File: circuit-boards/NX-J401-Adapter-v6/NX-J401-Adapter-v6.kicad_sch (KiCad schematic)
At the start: 19 parts, among them J1 NX BUTTON, J2 POWER, J3 USB1, J4 USB2, J5 CAN1, J6 CAN1, J7 15V, Q1 SQM120P06-07L_GE3, SW1 RECOVERY, SW2 RESET

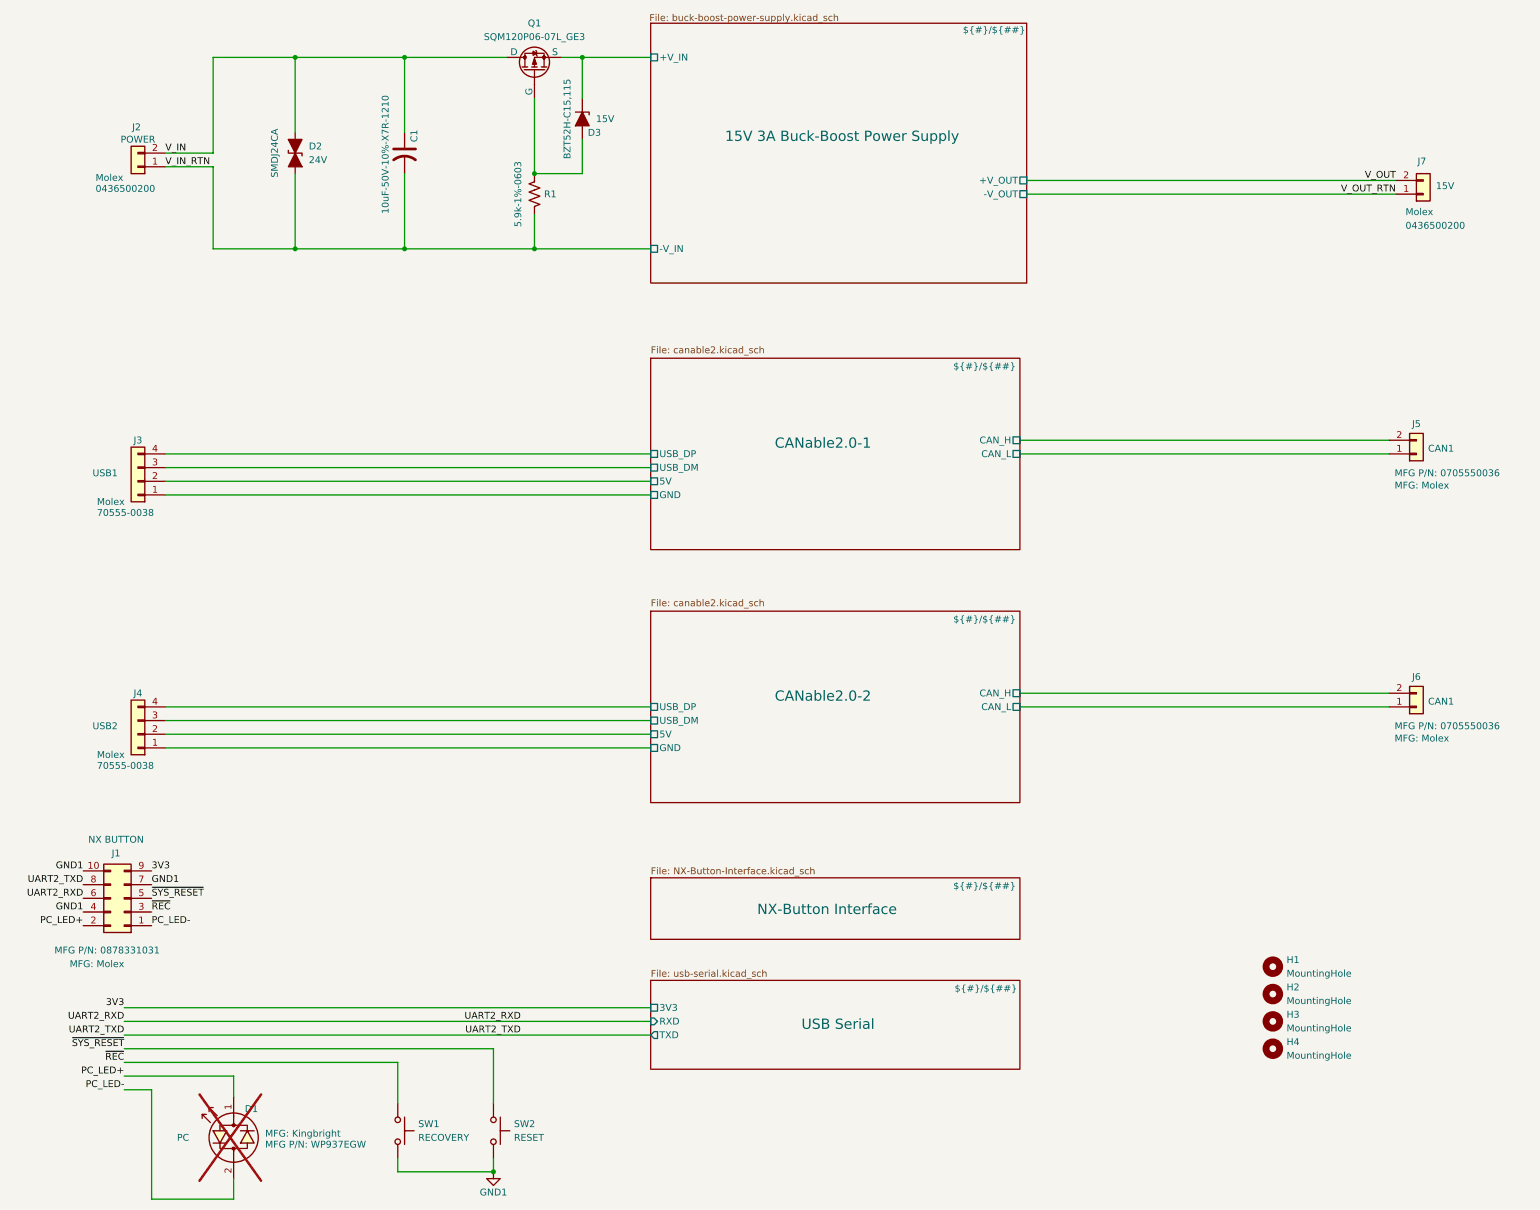
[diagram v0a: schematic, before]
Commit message: Changed canable to use 3.3V power form USB to use key-e connector that breaks out USB and 3V3
Signed-off-by: Scott Berman <sgberman1@gmail.com>
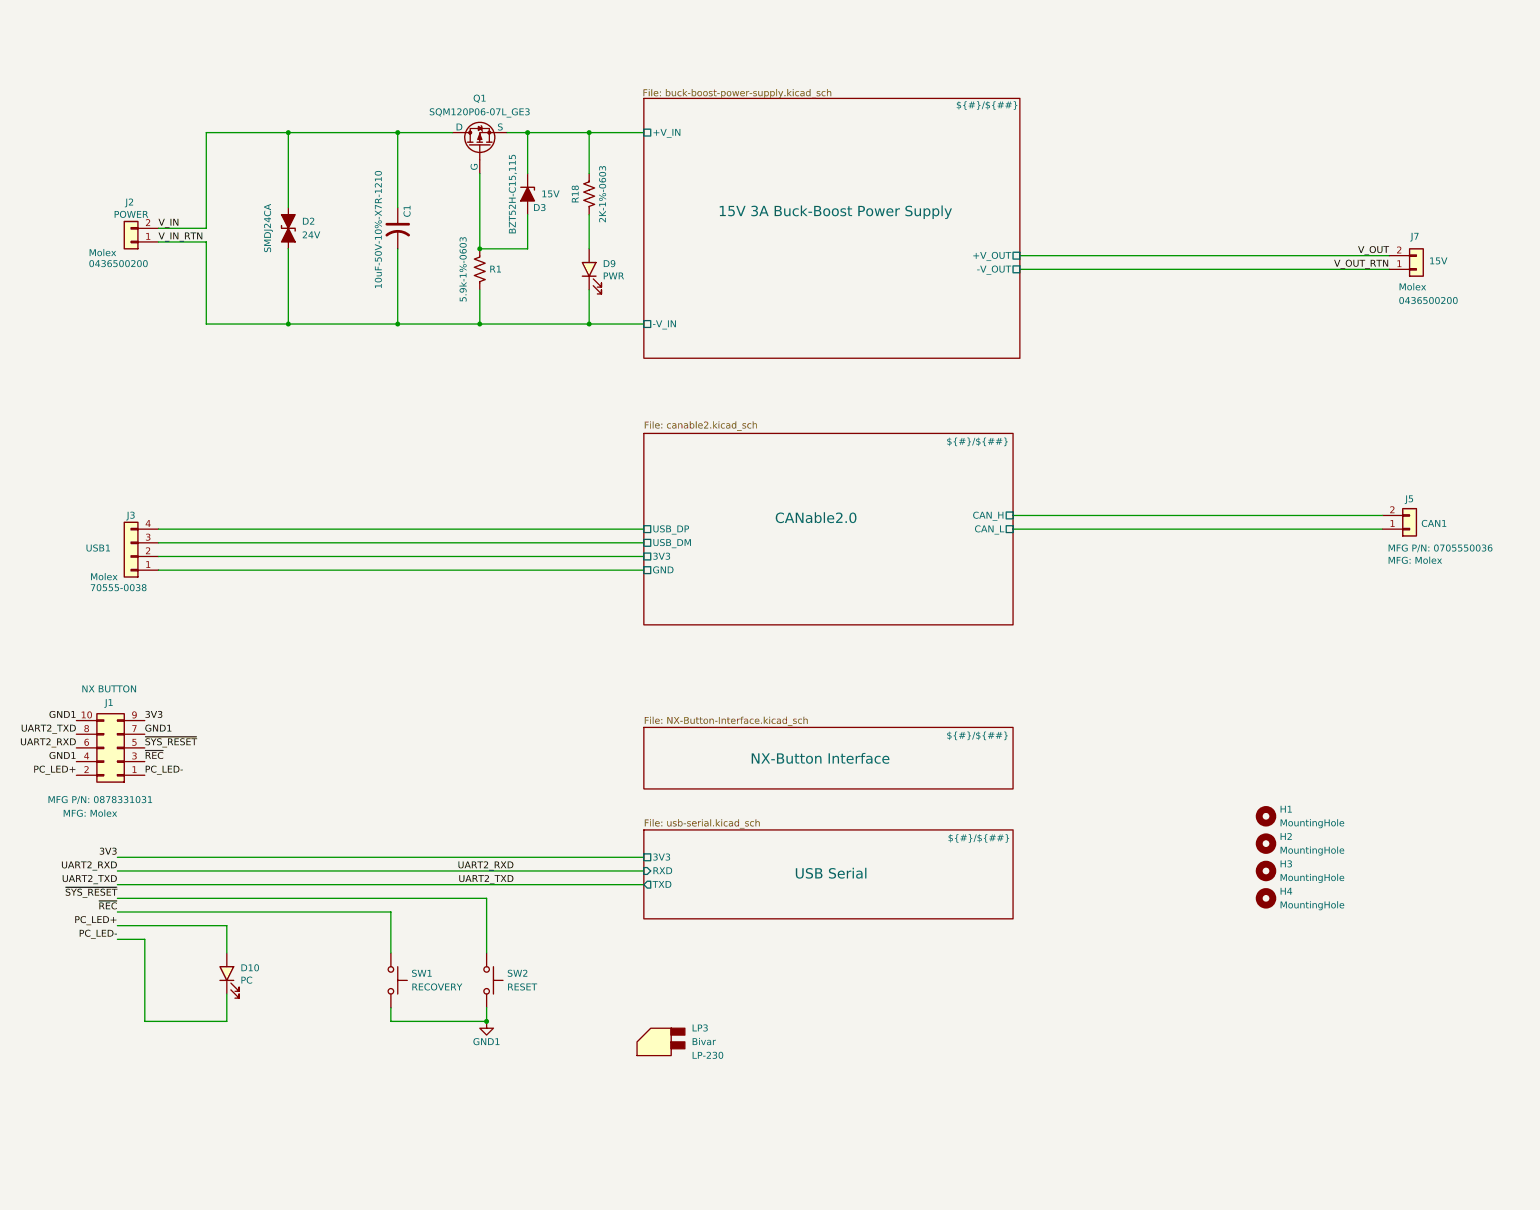
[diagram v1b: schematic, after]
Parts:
- removed D1: PC, LED_THT:LED_D3.0mm_Horizontal_O1.27mm_Z2.0mm, symbol Device:LED_Dual_Bidirectional
- removed J4: USB2, NX-J401-Adapter:Molex-70555-0003, symbol Connector_Generic:Conn_01x04
- removed J6: CAN1, NX-J401-Adapter:Molex-70555-0001, symbol Connector_Generic:Conn_01x02
- added D10: PC, LED_SMD:LED_1206_3216Metric, symbol Device:LED
- added D9: PWR, LED_SMD:LED_1206_3216Metric, symbol Device:LED
- added LP3: (no value), NX-J401-Adapter:Bivar-LP-230, symbol NX-J401-Adapter:Light_Pipe
- added R18: 2K-1%-0603, Resistor_SMD:R_0603_1608Metric, symbol Device:R_US
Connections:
- net 15V 3A Buck-Boost Power Supply/+V_IN: now also R18.1
- net PC_LED+: now also D10.2 (A)
- net PC_LED-: now also D10.1 (K)
- net V_IN_RTN: now also D9.1 (K)
- net CANable2.0/5V renamed CANable2.0/3V3
- new net: D9.2 (A), R18.2
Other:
- sheet CANable2.0-1 renamed CANable2.0
- removed sheet CANable2.0-2
- sheet CANable2.0 ports: added 3V3; removed 5V
- moved on the sheet: C1, D2, D3, H1, H2, H3, H4, J1, J2, J3, J5, J7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

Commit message: WIP update
Signed-off-by: Scott Berman <sgberman1@gmail.com>
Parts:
- removed J1: NX BUTTON, NX-J401-Adapter:Molex-0878331031, symbol Connector_Generic:Conn_02x05_Odd_Even
- added J10: NX CONTROL & UART, Connector_PinHeader_2.54mm:PinHeader_1x18_P2.54mm_Horizontal, symbol Connector:Conn_01x18_Pin
- added J4, J6: Terminal, NX-J401-Adapter:Keystone-7774, symbol NX-J401-Adapter:Keystone-7774
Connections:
- net UART2_RXD: now also J10.9 (Pin_9)
- net UART2_TXD: now also J10.10 (Pin_10)
- net ~{REC}: now also J10.16 (Pin_16)
- net ~{SYS_RESET}: now also J10.14 (Pin_14)
- new net 3V3_BTN: J10.4 (Pin_4)
- new net CAN_RX: J10.2 (Pin_2)
- new net CAN_TX: J10.1 (Pin_1)
- new net GND_BTN: J10.13 (Pin_13), J10.15 (Pin_15), J10.3 (Pin_3)
- new net NX_PC_LED+: J10.8 (Pin_8)
- new net NX_PC_LED-: J10.7 (Pin_7)
- no-connect marks 0 -> 6
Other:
- note added: "AC OK"
- note added: "Auto Power On Disable"
- note added: "GND"
- note added: "SLEEP/WAKE*"

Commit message: Changed USB header ot pico lock and light pipe to single row
Signed-off-by: Scott Berman <sgberman1@gmail.com>
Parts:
- removed LP3: (no value), NX-J401-Adapter:Bivar-LP-230, symbol NX-J401-Adapter:Light_Pipe
- added D1: STPS20M100SG-TR, Package_TO_SOT_SMD:TO-263-2, symbol Device:D_Schottky_AAK
- added LP1: (no value), NX-J401-Adapter:Bivar-RLP4-200-500, symbol NX-J401-Adapter:Bivar-RLP4-200-500
- J3: footprint NX-J401-Adapter:Molex-70555-0003 -> NX-J401-Adapter:Molex-PicoLatch-5040500491; DIST P/N WM4177-ND -> WM10137CT-ND; JLCPCB P/N (none) -> C177235; MFG P/N 70555-0038 -> 5040500491
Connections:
- net V_OUT: now also D1.2 (K)
- new net 15V 3A Buck-Boost Power Supply/+V_OUT: D1.1 (A), D1.3 (A)

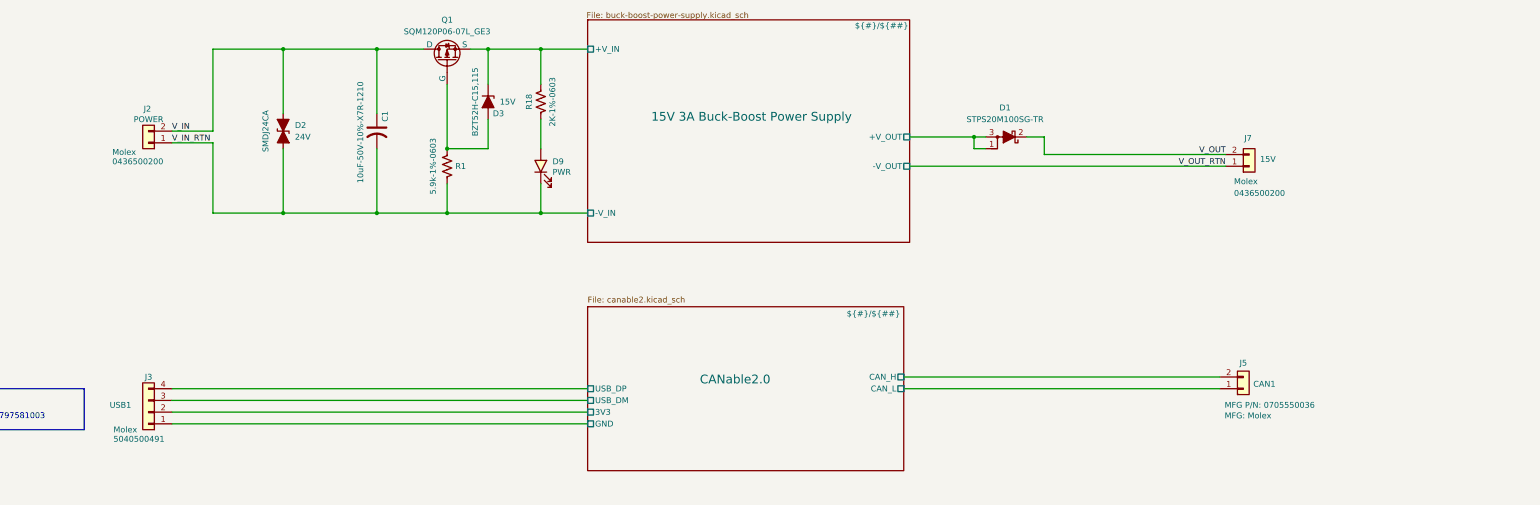
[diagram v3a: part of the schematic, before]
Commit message: Added ideal diode circuit for reverse polarity and output or-ing
Signed-off-by: Scott Berman <sgberman1@gmail.com>
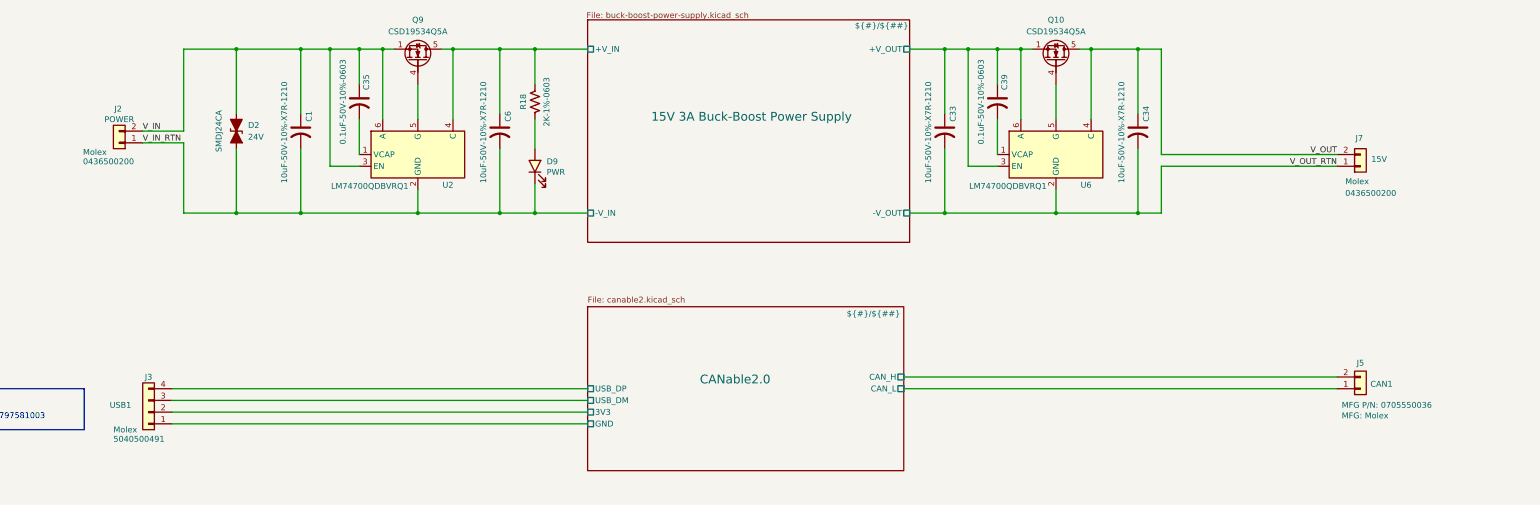
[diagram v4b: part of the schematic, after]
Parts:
- removed D1: STPS20M100SG-TR, Package_TO_SOT_SMD:TO-263-2, symbol Device:D_Schottky_AAK
- removed D3: 15V, Diode_SMD:D_SOD-123F, symbol Device:D_Zener
- removed Q1: SQM120P06-07L_GE3, NX-J401-Adapter:TO-263-2, symbol NX-AdapterBoard:SQM40061EL_GE3
- removed R1: 5.9k-1%-0603, Resistor_SMD:R_0603_1608Metric, symbol Device:R_US
- added C33, C34, C6: 10uF-50V-10%-X7R-1210, Capacitor_SMD:C_1210_3225Metric, symbol Device:C_US
- added C35, C39: 0.1uF-50V-10%-0603, Capacitor_SMD:C_0603_1608Metric, symbol Device:C_US
- added Q10, Q9: CSD19534Q5A, NX-J401-Adapter:TI-SON5x6, symbol Transistor_FET:CSD19534Q5A
- added U2, U6: LM74700QDBVRQ1, Package_TO_SOT_SMD:SOT-23-6, symbol NX-J401-Adapter:TI-LM74700QDBVRQ1
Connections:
- net 15V 3A Buck-Boost Power Supply/+V_IN: now also C6.1, Q9.5 (D), U2.4 (C)
- net 15V 3A Buck-Boost Power Supply/+V_OUT: now also C33.1, C39.1, Q10.1 (S), Q10.2 (S), Q10.3 (S), U6.3 (EN), U6.6 (A)
- net V_IN: now also C35.1, Q9.1 (S), Q9.2 (S), Q9.3 (S), U2.3 (EN), U2.6 (A)
- net V_IN_RTN: now also C6.2, U2.2 (GND)
- net V_OUT: now also C34.1, Q10.5 (D), U6.4 (C)
- net V_OUT_RTN: now also C33.2, C34.2, U6.2 (GND)
- new net: C35.2, U2.1 (VCAP)
- new net: Q9.4 (G), U2.5 (G)
- new net: C39.2, U6.1 (VCAP)
- new net: Q10.4 (G), U6.5 (G)
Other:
- moved on the sheet: C1, D2, D9, J2, J5, J7, R18

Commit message: Starting component placement
Signed-off-by: Scott Berman <sgberman1@gmail.com>
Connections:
- net 15V 3A Buck-Boost Power Supply/+V_IN renamed VIN_PS
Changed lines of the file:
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@@
-	(wire
-		(pts
-			(xy 168.91 45.72) (xy 180.34 45.72)
-		)
-		(stroke
-			(width 0)
-			(type default)
-		)
-	)
 	(wire
 		(pts
@@
 	(wire
 		(pts
-			(xy 161.29 45.72) (xy 168.91 45.72)
+			(xy 161.29 45.72) (xy 180.34 45.72)
 		)
 		(stroke
@@
 		)
 	)
+	(label "VIN_PS"
+		(at 177.8 45.72 180)
+		(effects
+			(font
+				(size 1.27 1.27)
+			)
+			(justify right bottom)
+		)
+	)

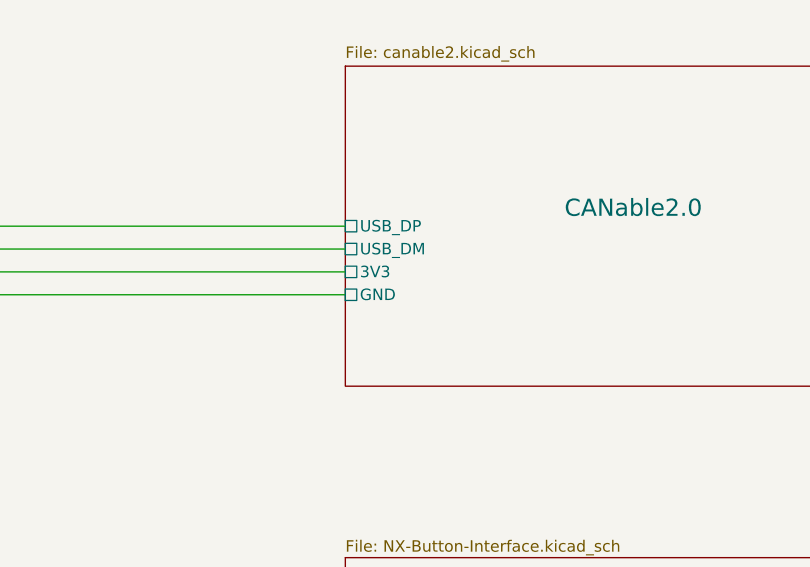
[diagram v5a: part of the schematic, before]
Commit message: Improved placement.  Pre-routing
Signed-off-by: Scott Berman <sgberman1@gmail.com>
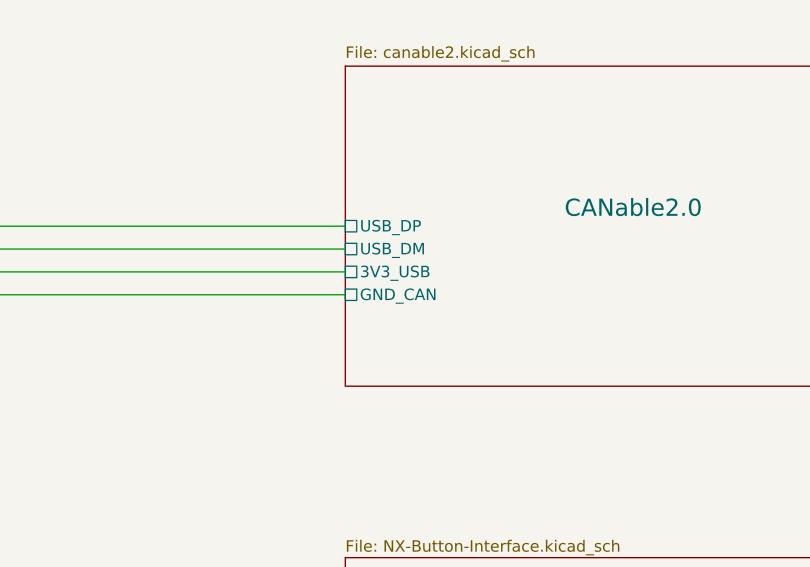
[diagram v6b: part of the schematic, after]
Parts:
- J10: DIST (none) -> Digikey; DIST P/N (none) -> 2057-PH1RB-18-UA-ND; MFG (none) -> Adam Tech; MFG P/N (none) -> PH1RB-18-UA
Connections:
- net CANable2.0/3V3 renamed CANable2.0/3V3_USB
- net CANable2.0/GND renamed CANable2.0/GND_CAN
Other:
- sheet CANable2.0 ports: added 3V3_USB, GND_CAN; removed 3V3, GND
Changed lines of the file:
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@@
 	(wire
 		(pts
-			(xy 248.92 116.84) (xy 342.9 116.84)
-		)
-		(stroke
-			(width 0)
-			(type default)
-		)
-	)
-	(wire
-		(pts
 			(xy 299.72 81.28) (xy 304.8 81.28)
 		)
@@
 	(wire
 		(pts
+			(xy 248.92 116.84) (xy 342.9 116.84)
+		)
+		(stroke
+			(width 0)
+			(type default)
+		)
+	)
+	(wire
+		(pts
 			(xy 262.89 71.12) (xy 262.89 45.72)
 		)
@@
 			)
 		)
-		(property "Datasheet" ""
+		(property "Datasheet" "Components/Adam-Tech-ph1rb-xx-ua.pdf"
 			(at 39.37 187.96 0)
 			(hide yes)
@@
 			)
 		)
-		(property "Description" "Generic connector, single row, 01x18, script generated"
+		(property "Description" "CONN HEADER R/A 18POS 2.54MM"
+			(at 39.37 187.96 0)
+			(hide yes)
+			(show_name no)
+			(do_not_autoplace no)
+			(effects
+				(font
+					(size 1.27 1.27)
+				)
+			)
+		)
+		(property "MFG" "Adam Tech"
+			(at 39.37 187.96 0)
+			(hide yes)
+			(show_name no)
+			(do_not_autoplace no)
+			(effects
+				(font
+					(size 1.27 1.27)
+				)
+			)
+		)
+		(property "MFG P/N" "PH1RB-18-UA"
+			(at 39.37 187.96 0)
+			(hide yes)
+			(show_name no)
+			(do_not_autoplace no)
+			(effects
+				(font
+					(size 1.27 1.27)
+				)
+			)
+		)
+		(property "DIST" "Digikey"
+			(at 39.37 187.96 0)
+			(hide yes)
+			(show_name no)
+			(do_not_autoplace no)
+			(effects
+				(font
+					(size 1.27 1.27)
+				)
+			)
+		)
+		(property "DIST P/N" "2057-PH1RB-18-UA-ND"
 			(at 39.37 187.96 0)
 			(hide yes)
@@
 			)
 		)
-		(pin "GND" passive
-			(at 180.34 127 180)
+		(pin "USB_DM" passive
+			(at 180.34 121.92 180)
 			(effects
 				(font
@@
 			)
 		)
-		(pin "USB_DM" passive
-			(at 180.34 121.92 180)
+		(pin "USB_DP" passive
+			(at 180.34 119.38 180)
 			(effects
 				(font
@@
 			)
 		)
-		(pin "USB_DP" passive
-			(at 180.34 119.38 180)
+		(pin "3V3_USB" passive
+			(at 180.34 124.46 180)
 			(effects
 				(font
@@
 			)
 		)
-		(pin "3V3" passive
-			(at 180.34 124.46 180)
+		(pin "GND_CAN" passive
+			(at 180.34 127 180)
 			(effects
 				(font
